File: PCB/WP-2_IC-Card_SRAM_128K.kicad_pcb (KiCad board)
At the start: 2 copper layers, 54 x 54 mm, 15 parts, among them J1 SMS-138-01-G-S, U1 628128_TSOP

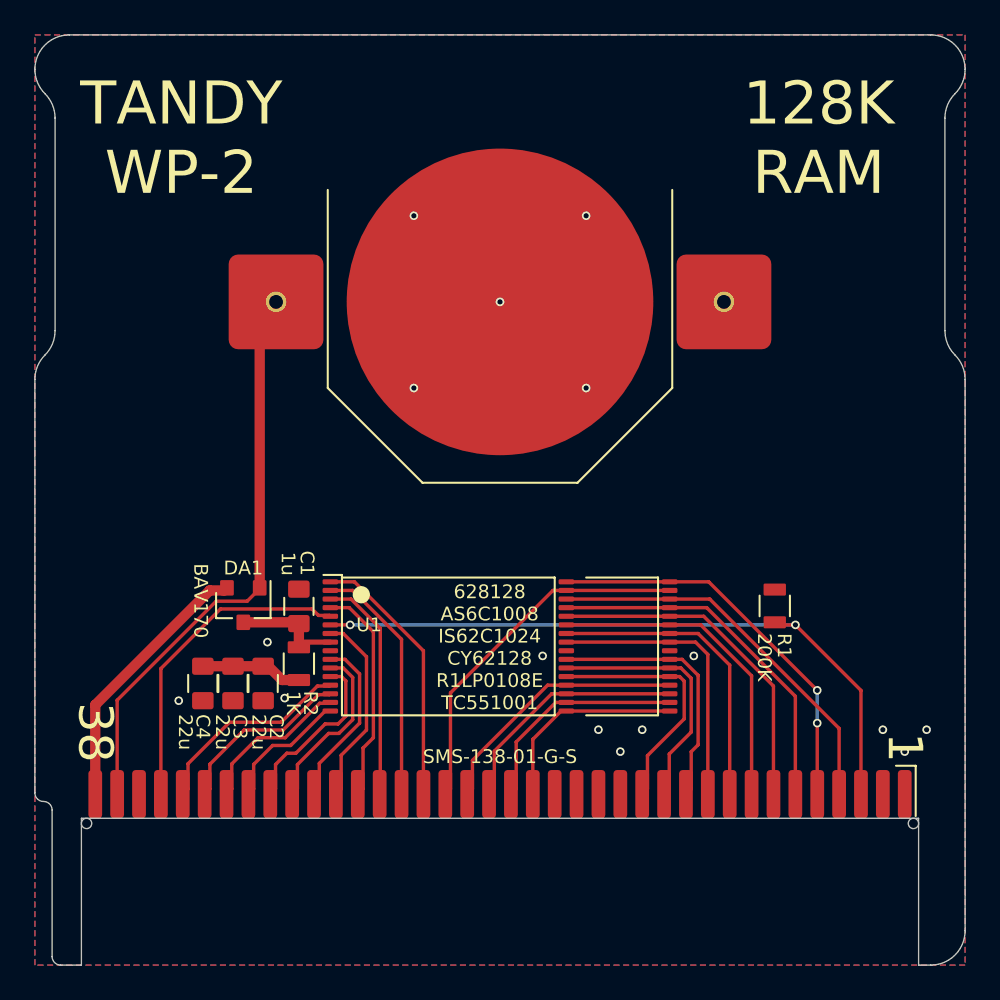
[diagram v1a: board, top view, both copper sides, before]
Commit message: local symbol & footprint library organization, add shielded mram version
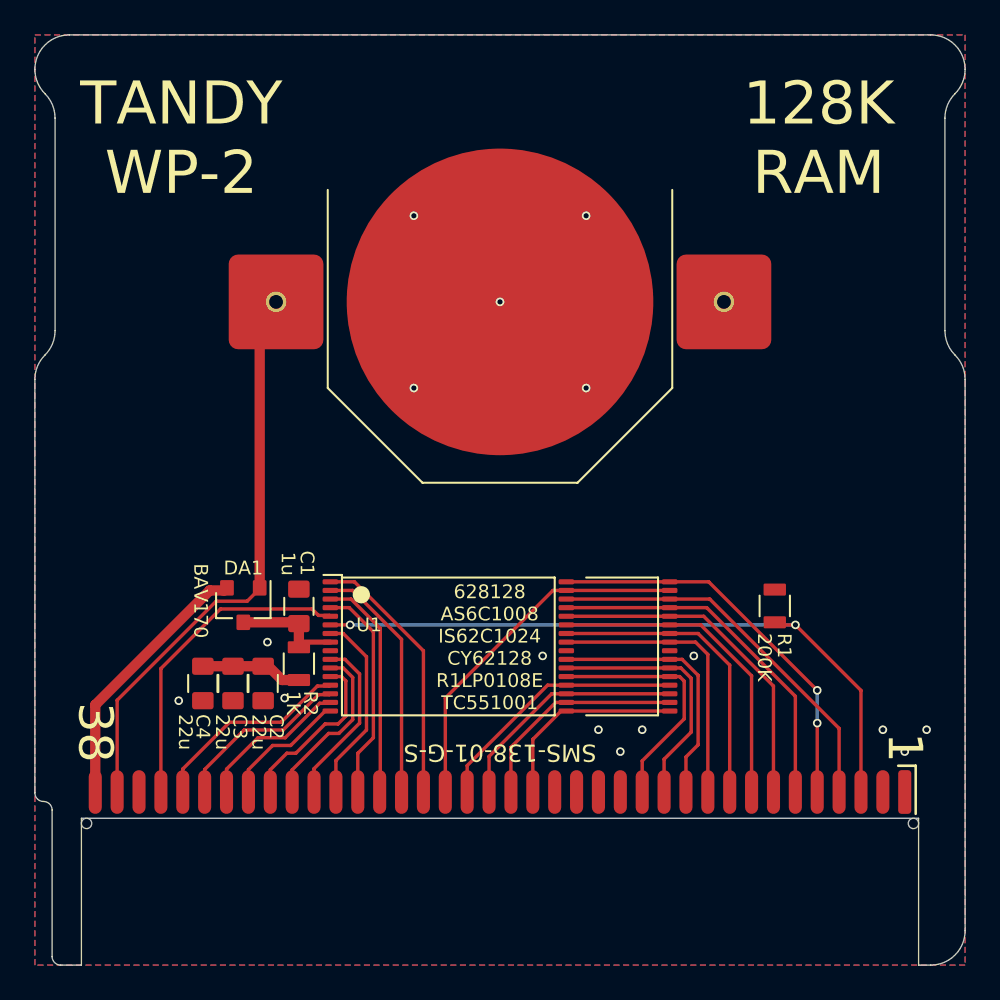
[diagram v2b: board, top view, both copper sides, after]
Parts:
- removed the REF** at (135.9, 95.2)
- removed corner1, corner2: npth_0.6mm, 0_LOCAL:npth_0.6mm
- added N1: WP-2_IC-Card_Cover_SRAM, 000_LOCAL:WP-2_IC_Card_Cover_RAM, F.Cu at (135.9, 95.2)
- added REF**: npth_0.6mm, 000_LOCAL:npth_0.6mm, F.Cu at (112.0, 114.0)
- added REF**: npth_0.6mm, 000_LOCAL:npth_0.6mm, F.Cu at (159.9, 114.0)
- BT1: footprint 0_LOCAL:2016_battery_holder_smt -> 000_LOCAL:2016_battery_holder_smt
- C1, C2, C3, C4: footprint 0_LOCAL:C_0805_1mm -> 000_LOCAL:C_0805_1mm
- DA1: footprint 0_LOCAL:SOT-23 -> 000_LOCAL:SOT-23
- J1: footprint 0_LOCAL:SMS-138-01-x-x_edge -> 000_LOCAL:SMS-138-01-x-x_pcb_edge
- R1, R2: footprint 0_LOCAL:R_0805 -> 000_LOCAL:R_0805
- U1: footprint 0_LOCAL:TSOP32-dual -> 000_LOCAL:TSOP32-dual
- nail1, nail2: footprint 0_LOCAL:pth_nail -> 000_LOCAL:pth_nail
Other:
- board text added: "BOARD OUTLINE"
- board text removed: "drill to sharpen the inside corner"

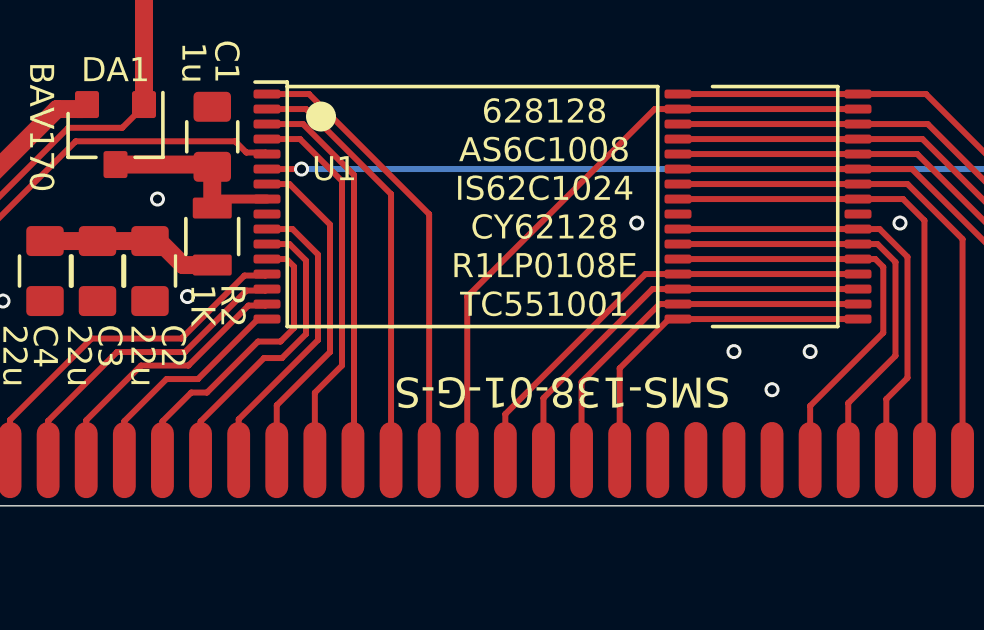
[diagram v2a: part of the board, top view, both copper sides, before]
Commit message: cleanup names, cover inside corner reliefs
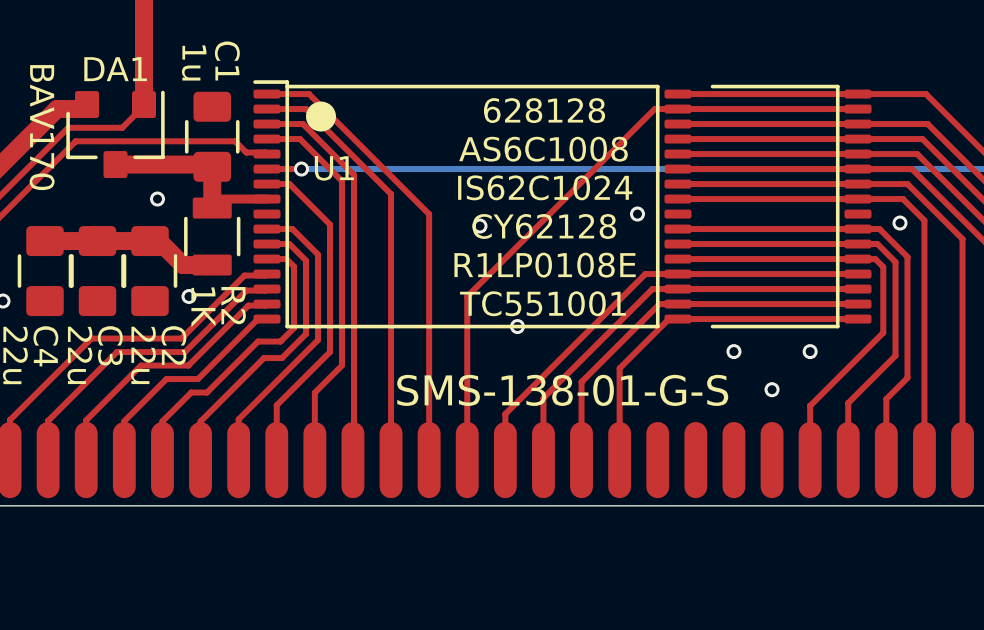
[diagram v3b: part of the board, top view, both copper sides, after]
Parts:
- N1: footprint 000_LOCAL:WP-2_IC_Card_Cover_RAM -> 000_LOCAL:WP-2_IC-Card_Cover_SRAM
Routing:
- net GND: vias 16 -> 18

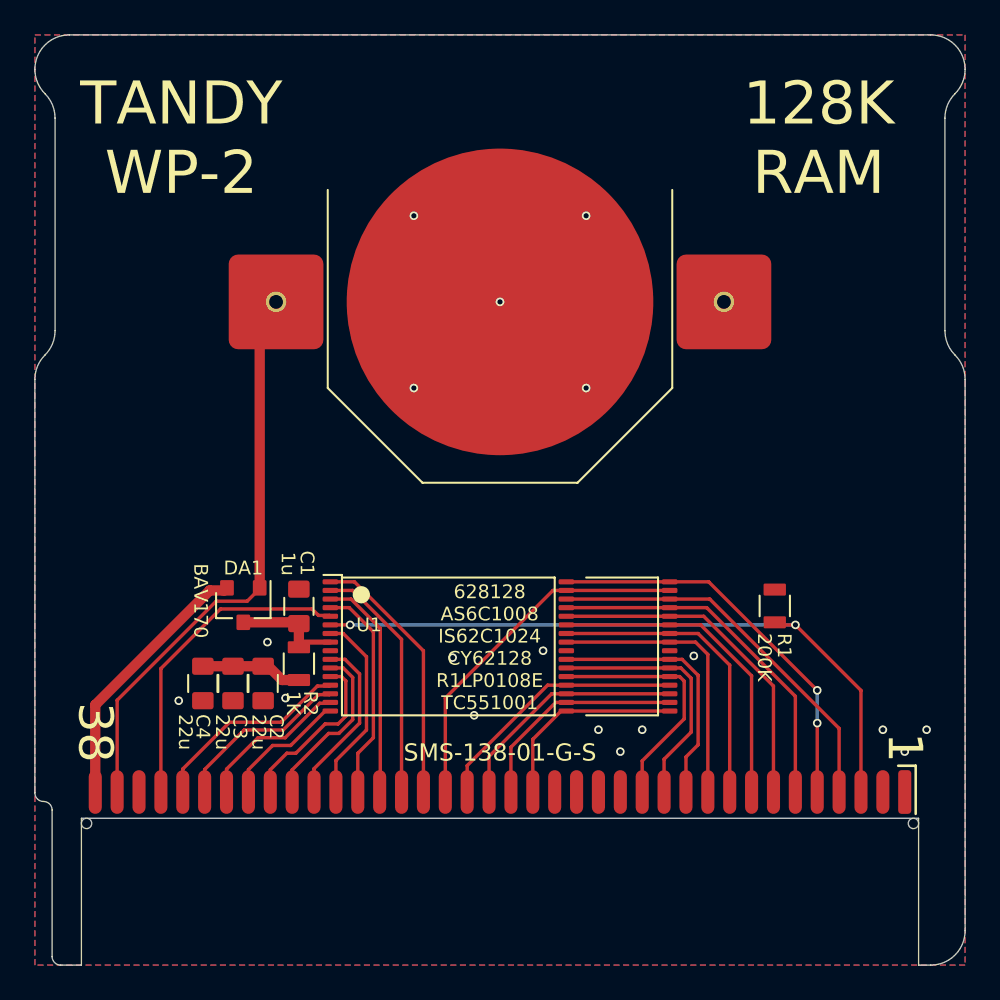
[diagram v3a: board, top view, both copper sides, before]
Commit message: redraw board outline and copy to all boards
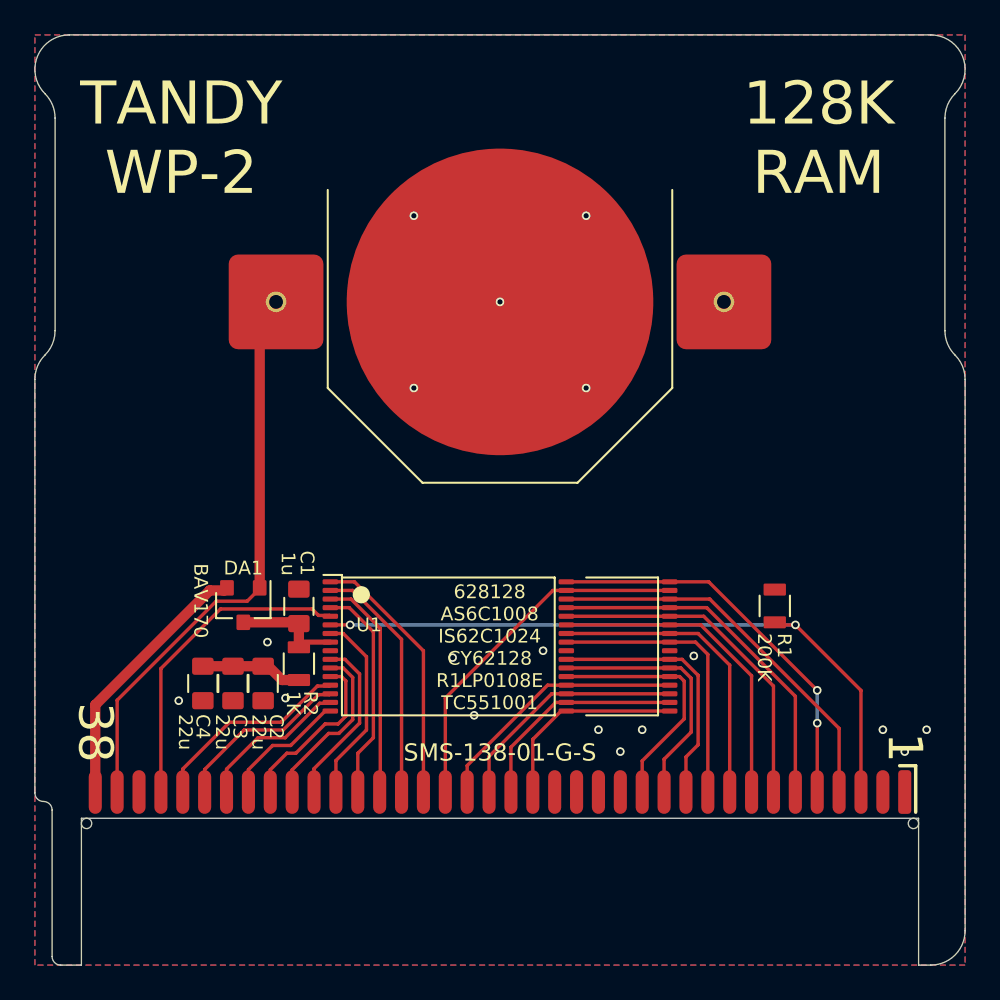
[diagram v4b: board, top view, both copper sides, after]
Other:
- outline, holes or cut-outs redrawn

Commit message: rom wren sw, boms, footprints, shielded mram
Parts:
- removed C4: 22u, 000_LOCAL:C_0805_1mm
- removed R2: 1K, 000_LOCAL:R_0805
- added REF**: Fiducial_1.5, 000_LOCAL:Fiducial_1.5, F.Cu at (160.9, 70.2)
- added REF**: Fiducial_1.5, 000_LOCAL:Fiducial_1.5, F.Cu at (110.5, 111.4)
- added REF**: Fiducial_1.5, 000_LOCAL:Fiducial_1.5, F.Cu at (111.0, 70.2)
- BT1: value CR2016 3v -> CR2016
- C1: footprint 000_LOCAL:C_0805_1mm -> 000_LOCAL:C_0805
- C2, C3: footprint 000_LOCAL:C_0805_1mm -> 000_LOCAL:C_1206
- moved U1 3.35 mm to (132.6, 103.7)
- moved C1 3.25 mm to (123.9, 104.6), turned to -90 degrees
- moved C3 2.45 mm to (118.0, 105.7)
- moved C2 1.21 mm to (121.0, 105.7)
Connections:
- C2 pad 1: Net-(C2-Pad1) -> VMEM
- C3 pad 1: Net-(C2-Pad1) -> VMEM
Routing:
- net Net-(C2-Pad1): track 5.91 -> 0.00 mm
- net VMEM: track 6.76 -> 10.7 mm
- net /VBUS: track 15.5 -> 16.4 mm
- net /VBAT: track 33.3 -> 34.2 mm
- net /~{WE}: track 18.6 -> 19.5 mm
- net /D5: track 15.1 -> 15.8 mm
- net /~{OE}: track 23.1 -> 23.8 mm
- net /~{CE1}: track 22.6 -> 23.3 mm
- net /D4: track 16.5 -> 17.2 mm
- net /D3: track 17.6 -> 18.3 mm
- net /D2: track 18.7 -> 19.4 mm
- net /D1: track 19.9 -> 20.6 mm
- net /D0: track 21.0 -> 21.7 mm
- net /D6: track 14.8 -> 15.4 mm
- net GND: vias 18 -> 19

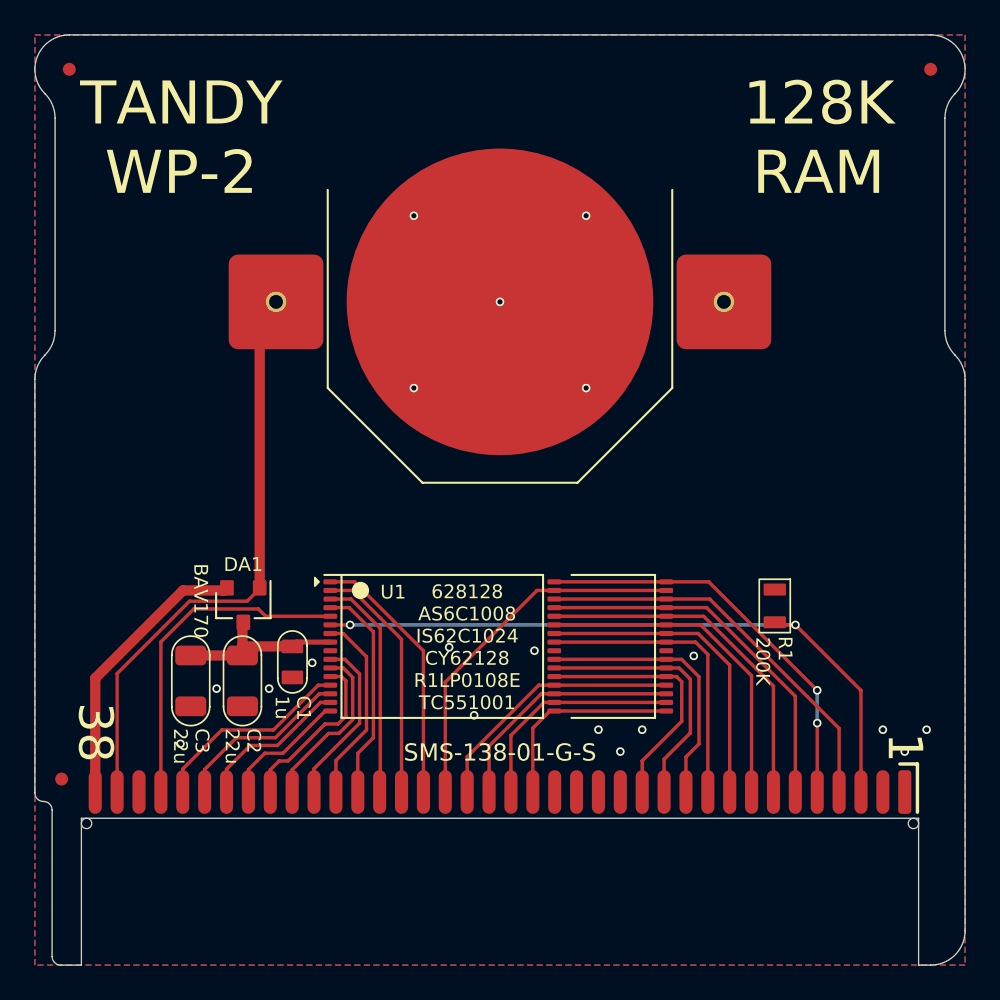
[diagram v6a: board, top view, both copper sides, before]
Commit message: SRAM compatible with 512K, pullup /WE, TSOP32 footprint, cfg jumpers
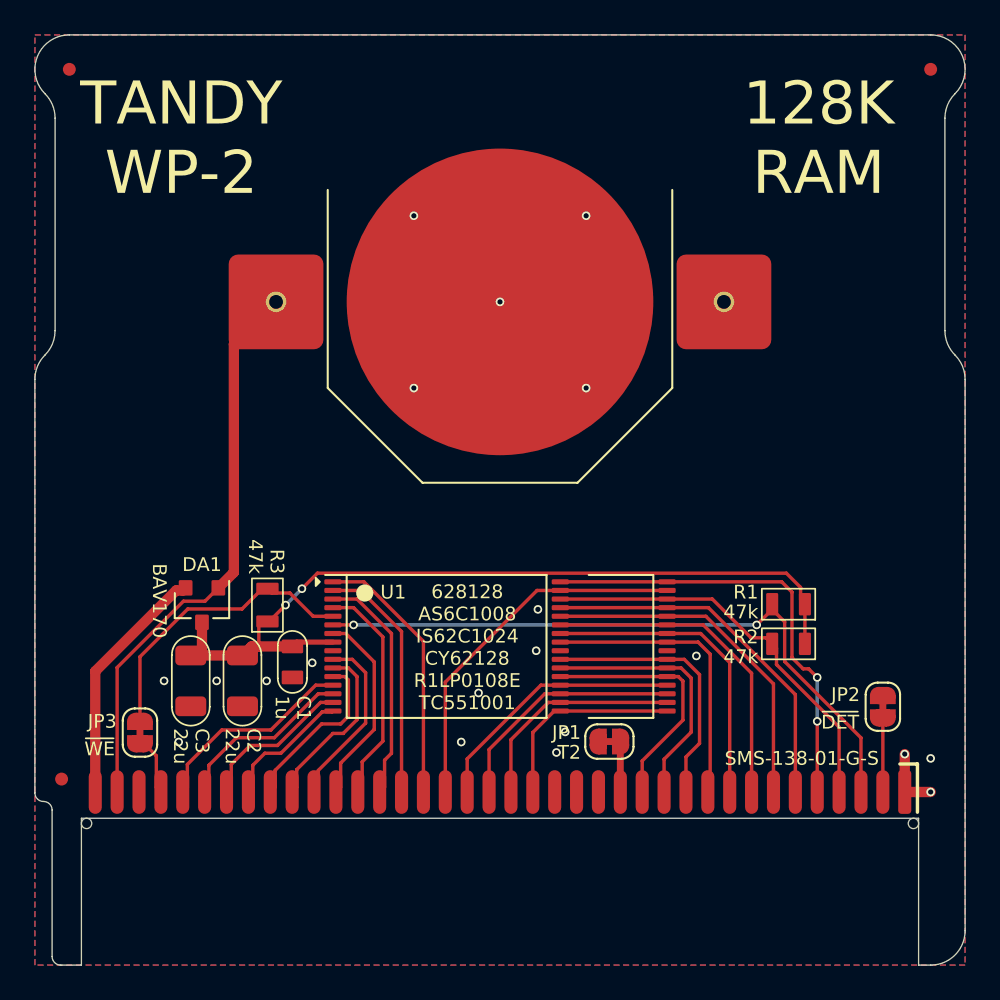
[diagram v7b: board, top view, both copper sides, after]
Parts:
- added JP1: T2, 000_LOCAL:SolderJumper-2_P1.3mm_Bridged_RoundedPad1.0x1.5mm, F.Cu at (142.3, 109.3)
- added JP2: ~{DET}, 000_LOCAL:SolderJumper-2_P1.3mm_Bridged_RoundedPad1.0x1.5mm, F.Cu at (158.2, 107.2)
- added JP3: ~{WE}, 000_LOCAL:SolderJumper-2_P1.3mm_Bridged_RoundedPad1.0x1.5mm, F.Cu at (115.0, 108.7)
- added R2: 47k, 000_LOCAL:R_0805, F.Cu at (152.7, 103.6)
- added R3: 47k, 000_LOCAL:R_0805, F.Cu at (122.5, 101.3)
- R1: value 200K -> 47k
- moved U1 3.35 mm to (135.9, 103.7)
- moved DA1 2.40 mm to (118.7, 101.3)
- moved R1 0.81 mm to (152.7, 101.3), turned to 180 degrees
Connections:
- net /VBAT renamed +BATT
- J1 pad 14: GND -> /T2
- J1 pad 15: unconnected-(J1-Pin_15-Pad15) -> /S1
- J1 pad 16: unconnected-(J1-Pin_16-Pad16) -> /S2
- J1 pad 17: unconnected-(J1-Pin_17-Pad17) -> /A17
- J1 pad 2: GND -> /~{DET}
- J1 pad 35: /~{WE} -> /R/~{W}
- J1 pad 36: unconnected-(J1-Pin_36-Pad36) -> /S3
- R1 pad 1: GND -> VMEM
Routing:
- net VMEM: track 10.7 -> 48.4 mm, vias 0 -> 2
- net /~{DET}: track 0.00 -> 4.30 mm
- net GND: track 0.00 -> 3.71 mm, vias 19 -> 20
- net /R/~{W}: track 0.00 -> 3.45 mm
- net /T2: track 0.00 -> 2.94 mm
- net /~{OE}: track 23.8 -> 26.1 mm
- net /~{WE}: track 19.5 -> 17.2 mm
- net /VBUS: track 16.4 -> 14.3 mm
- net +BATT: track 34.2 -> 33.0 mm
- net /A9: track 13.1 -> 13.7 mm

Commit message: refactor cover scad more, cover models makefile, adjust new sram switch & batt positions
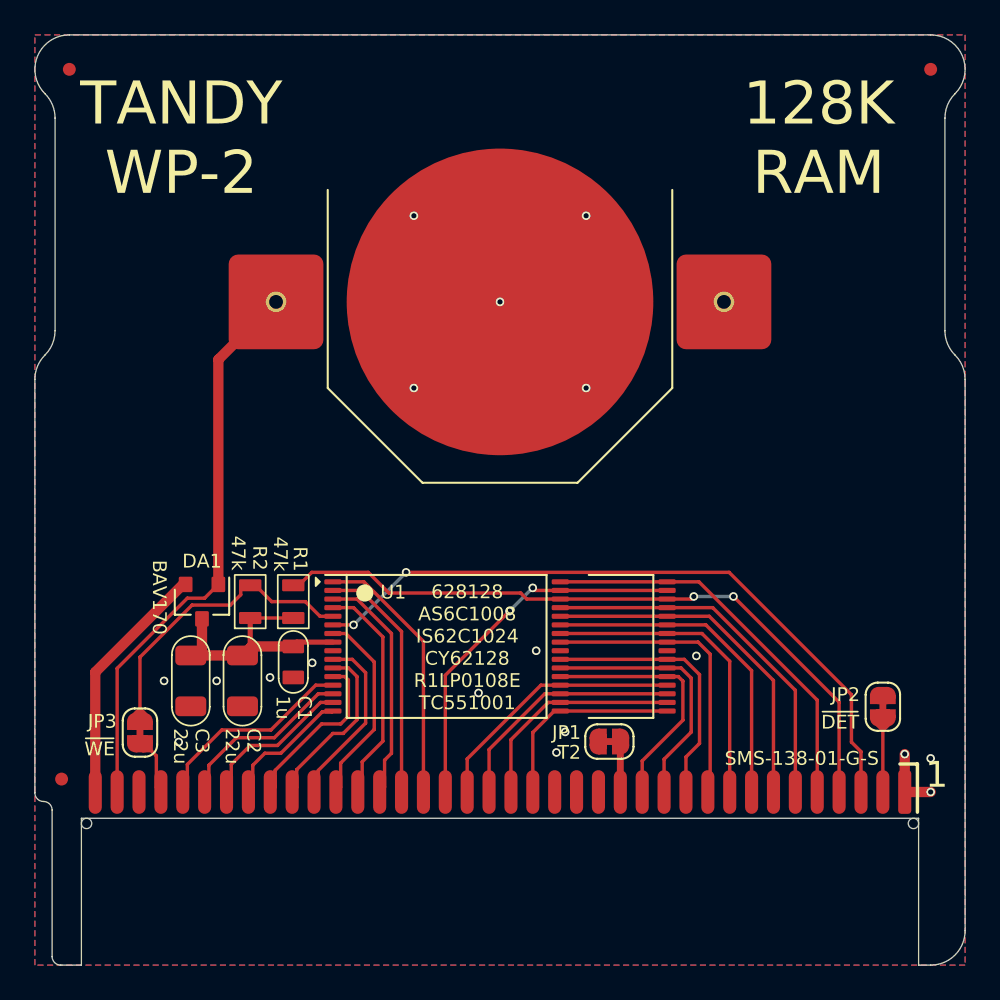
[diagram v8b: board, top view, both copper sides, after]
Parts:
- removed the R1 at (152.7, 101.3)
- N1: value WP-2_IC-Card_Cover_SRAM -> WP-2_IC-Card_Cover_SRAM_128K; footprint 000_LOCAL:WP-2_IC-Card_Cover_SRAM -> 000_LOCAL:WP-2_IC-Card_Cover_SRAM_128K
- moved R1 28.9 mm to (124.0, 101.1), turned to 90 degrees
- moved R2 1.02 mm to (121.5, 101.1)
- moved DA1 0.20 mm to (118.7, 101.1)
- renumbered R2 to R1, R3 to R2
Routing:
- net VMEM: track 48.4 -> 15.5 mm, vias 2 -> 0
- net /~{CE1}: track 23.6 -> 40.5 mm, vias 0 -> 2
- net /~{OE}: track 26.1 -> 23.1 mm, vias 2 -> 0
- net /CE2: track 39.2 -> 40.2 mm
- net /A12: track 21.5 -> 21.8 mm, vias 0 -> 2
- net GND: vias 20 -> 18
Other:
- board text removed: "38"
